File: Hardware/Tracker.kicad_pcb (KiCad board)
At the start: 2 copper layers, 233.7 x 114.2 mm, 58 parts, among them J1 Battery, J10 132134, J11 SPI_Programming, J2 Motor, J3 Wind, J4 RX, J5 TX, J6 GND, J7 GND, J8 GND, J9 Haeder_LED, U1 L7805, U2 ATmega328P-P, U3 LM317_TO-220, U4 L298N, U5 74HC123, U6 LM358, U7 GK9501, Y1 16MHz

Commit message: Update of PCB
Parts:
- removed D6: LED_RBKG, Connector_PinHeader_1.27mm:PinHeader_1x04_P1.27mm_Vertical
- removed R23: 270, Resistor_THT:R_Axial_DIN0204_L3.6mm_D1.6mm_P5.08mm_Horizontal
- added C10: 100nF, Capacitor_THT:C_Rect_L7.0mm_W2.0mm_P5.00mm, F.Cu at (82.3, 68.1)
- added D11: 1N5406, Diode_THT:D_DO-201AD_P15.24mm_Horizontal, F.Cu at (108.5, 116.6)
- added D12: 3.3V, Diode_THT:D_A-405_P10.16mm_Horizontal, F.Cu at (29.7, 86.9)
- added D13: LED, LED_THT:LED_D3.0mm, F.Cu at (54.9, 76.7)
- added J12: Sortie Moteur, TerminalBlock_Phoenix:TerminalBlock_Phoenix_MKDS-1,5-2-5.08_1x02_P5.08mm_Horizontal, F.Cu at (44.7, 127.3)
- added J13: Position_Potentiometer, TerminalBlock_Phoenix:TerminalBlock_Phoenix_MKDS-1,5-3-5.08_1x03_P5.08mm_Horizontal, F.Cu at (24.4, 76.2)
- added Q1: IRF4905, Package_TO_SOT_THT:TO-220-3_Vertical, F.Cu at (36.3, 102.4)
- added Q2: IRF520, Package_TO_SOT_THT:TO-220-3_Vertical, F.Cu at (34.2, 114.0)
- added Q4: IRF4905, Package_TO_SOT_THT:TO-220-3_Vertical, F.Cu at (61.5, 105.2)
- added Q5: IRF520, Package_TO_SOT_THT:TO-220-3_Vertical, F.Cu at (59.8, 113.9)
- added Q6: IRF4905, Package_TO_SOT_THT:TO-220-3_Vertical, F.Cu at (47.9, 90.9)
- added R13: 470, Resistor_THT:R_Axial_DIN0207_L6.3mm_D2.5mm_P7.62mm_Horizontal, F.Cu at (14.2, 103.4)
- added R16: 470, Resistor_THT:R_Axial_DIN0207_L6.3mm_D2.5mm_P7.62mm_Horizontal, F.Cu at (163.2, 103.8)
- added R17: 2.2K, Resistor_THT:R_Axial_DIN0207_L6.3mm_D2.5mm_P7.62mm_Horizontal, F.Cu at (27.9, 96.0)
- added R18: 1K, Resistor_THT:R_Axial_DIN0207_L6.3mm_D2.5mm_P7.62mm_Horizontal, F.Cu at (24.1, 104.9)
- added R19: 100k, Resistor_THT:R_Axial_DIN0207_L6.3mm_D2.5mm_P7.62mm_Horizontal, F.Cu at (30.5, 116.3)
- added R20: 1K, Resistor_THT:R_Axial_DIN0207_L6.3mm_D2.5mm_P7.62mm_Horizontal, F.Cu at (31.2, 96.0)
- added R24: 470, Resistor_THT:R_Axial_DIN0207_L6.3mm_D2.5mm_P7.62mm_Horizontal, F.Cu at (16.3, 124.0)
- added R26: 3.3K, Resistor_THT:R_Axial_DIN0207_L6.3mm_D2.5mm_P7.62mm_Horizontal, F.Cu at (37.3, 86.4)
- added R27: 470, Resistor_THT:R_Axial_DIN0207_L6.3mm_D2.5mm_P7.62mm_Horizontal, F.Cu at (75.2, 84.6)
- added R28: 1K, Resistor_THT:R_Axial_DIN0207_L6.3mm_D2.5mm_P7.62mm_Horizontal, F.Cu at (66.3, 97.8)
- added R29: 470, Resistor_THT:R_Axial_DIN0207_L6.3mm_D2.5mm_P7.62mm_Horizontal, F.Cu at (13.2, 124.0)
- added R30: 2.2K, Resistor_THT:R_Axial_DIN0207_L6.3mm_D2.5mm_P7.62mm_Horizontal, F.Cu at (66.0, 104.9)
- added R31: 1K, Resistor_THT:R_Axial_DIN0207_L6.3mm_D2.5mm_P7.62mm_Horizontal, F.Cu at (66.3, 115.6)
- added R32: 100k, Resistor_THT:R_Axial_DIN0207_L6.3mm_D2.5mm_P7.62mm_Horizontal, F.Cu at (66.5, 119.1)
- added R33: 1k, Resistor_THT:R_Axial_DIN0207_L6.3mm_D2.5mm_P7.62mm_Horizontal, F.Cu at (51.3, 91.9)
- added R34: 2.7K, Resistor_THT:R_Axial_DIN0207_L6.3mm_D2.5mm_P7.62mm_Horizontal, F.Cu at (26.7, 83.6)
- added R35: 1K, Resistor_THT:R_Axial_DIN0207_L6.3mm_D2.5mm_P7.62mm_Horizontal, F.Cu at (26.7, 86.6)
- added R37: 2.2K, Resistor_THT:R_Axial_DIN0207_L6.3mm_D2.5mm_P7.62mm_Horizontal, F.Cu at (54.4, 84.3)
- added R38: 3.3K, Resistor_THT:R_Axial_DIN0207_L6.3mm_D2.5mm_P7.62mm_Horizontal, F.Cu at (57.7, 76.7)
- added U10: PC817, Package_DIP:DIP-4_W7.62mm, F.Cu at (64.8, 91.2)
- added U11: PC817, Package_DIP:DIP-4_W7.62mm, F.Cu at (67.1, 122.9)
- added U12: PC817, Package_DIP:DIP-4_W7.62mm, F.Cu at (65.0, 84.3)
- added U8: PC817, Package_DIP:DIP-4_W7.62mm, F.Cu at (19.3, 116.8)
- D2, D3: value D -> 1N4818
- D4, D5, D8: value 1N4148 -> 1N5406; footprint Diode_THT:D_DO-35_SOD27_P7.62mm_Horizontal -> Diode_THT:D_DO-201AD_P15.24mm_Horizontal
- D9: value 1N4148 -> LED; footprint Diode_THT:D_DO-35_SOD27_P7.62mm_Horizontal -> LED_THT:LED_D3.0mm
- J2: value Motor -> +24V
- R1, R10, R11, R12, R15, R2, R3, R4, R5, R6, R7, R8, R9: footprint Resistor_THT:R_Axial_DIN0204_L3.6mm_D1.6mm_P5.08mm_Horizontal -> Resistor_THT:R_Axial_DIN0207_L6.3mm_D2.5mm_P7.62mm_Horizontal
- R21, R22: footprint Resistor_THT:R_Axial_DIN0204_L3.6mm_D1.6mm_P5.08mm_Horizontal -> Resistor_THT:R_Axial_DIN0207_L6.3mm_D2.5mm_P10.16mm_Horizontal
- U4: value L298N -> PC817; footprint Package_TO_SOT_THT:TO-220-15_P2.54x2.54mm_StaggerOdd_Lead4.58mm_Vertical -> Package_DIP:DIP-4_W7.62mm
- moved U4 199.4 mm to (17.3, 96.0), turned to 0 degrees
- moved D9 186.3 mm to (40.4, 85.3), turned to 0 degrees
- moved J2 174.7 mm to (47.8, 76.7)
- moved H4 134.4 mm to (9.91, 146.1)
- moved H1 132.9 mm to (10.9, 54.1)
- moved D5 111.8 mm to (108.2, 103.9), turned to 0 degrees
- moved D4 96.1 mm to (123.4, 122.7), turned to 180 degrees
- moved D8 93.7 mm to (123.4, 110.0), turned to 180 degrees
- moved C4 72.5 mm to (104.8, 67.5)
- moved C7 72.5 mm to (113.7, 83.3)
- moved J3 72.5 mm to (89.2, 73.5)
- moved R10 72.5 mm to (108.5, 78.6)
- moved R11 72.5 mm to (113.6, 80.9)
- moved R12 72.5 mm to (121.1, 80.8)
- moved R15 72.5 mm to (122.7, 67.6)
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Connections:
- net /XTAL1 renamed /Crystal/XTAl_1
- net /XTAL2 renamed /Crystal/XTAl_2
- D4 pad 1: +BATT -> Net-(D4-K)
- D4 pad 2: Net-(D4-A) -> GND
- D5 pad 1: Net-(D4-A) -> +VCC_Motor
- D5 pad 2: GND -> Net-(D4-K)
- D8 pad 1: +BATT -> Net-(D11-A)
- D8 pad 2: Net-(D8-A) -> GND
- D9 pad 1: Net-(D8-A) -> Net-(D9-K)
- D9 pad 2: GND -> +VCC_Motor
- J2 pad 1: Net-(D8-A) -> +24V
- J2 pad 2: Net-(D4-A) -> GND
- U2 pad 11: Net-(U2-PD5) -> unconnected-(U2-PD5-Pad11)
- U2 pad 12: Net-(U2-PD6) -> unconnected-(U2-PD6-Pad12)
- U2 pad 13: Net-(U2-PD7) -> unconnected-(U2-PD7-Pad13)
- U2 pad 14: /GNSS/RX -> /GNSS/PPS
- U2 pad 15: /GNSS/TX -> /GNSS/RX
- U2 pad 16: /GNSS/PPS -> /GNSS/TX
- U2 pad 23: /Motors/EN_MOTOR -> /Motors/IN_B
- U2 pad 24: /Motors/IN2_MOTOR -> /Motors/IN_A
- U2 pad 25: /Motors/IN1_MOTOR -> /Motors/ENABLE
- U2 pad 26: unconnected-(U2-PC3-Pad26) -> /Motors/Pot_Measure
- U4 pad 1: GND -> Net-(R13-Pad2)
- U4 pad 2: Net-(D8-A) -> GND
- U4 pad 3: Net-(D4-A) -> GND
- U4 pad 4: +5V -> Net-(R17-Pad1)
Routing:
- net +VCC_Motor: track 0.00 -> 62.7 mm
- net /Motors/EN_MOTOR: track 53.9 -> 0.00 mm
- net /Motors/IN_B: track 0.00 -> 53.3 mm
- net Net-(D11-A): track 0.00 -> 51.9 mm
- net Net-(D4-K): track 0.00 -> 49.6 mm
- net /Motors/IN_A: track 0.00 -> 46.0 mm
- net +24V: track 0.00 -> 45.4 mm
- net /Motors/IN1_MOTOR: track 32.7 -> 0.00 mm
- net /Motors/ENABLE: track 0.00 -> 32.7 mm
- net /Motors/IN2_MOTOR: track 32.7 -> 0.00 mm
- net (no net): track 0.00 -> 18.8 mm
- net Net-(Q2-G): track 0.00 -> 16.4 mm
- net GND: track 31.7 -> 16.7 mm
- net Net-(D4-A): track 12.3 -> 0.00 mm
- net Net-(D8-A): track 9.48 -> 0.00 mm
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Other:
- board size 233.7 x 114.2 mm -> 204.5 x 104.5 mm

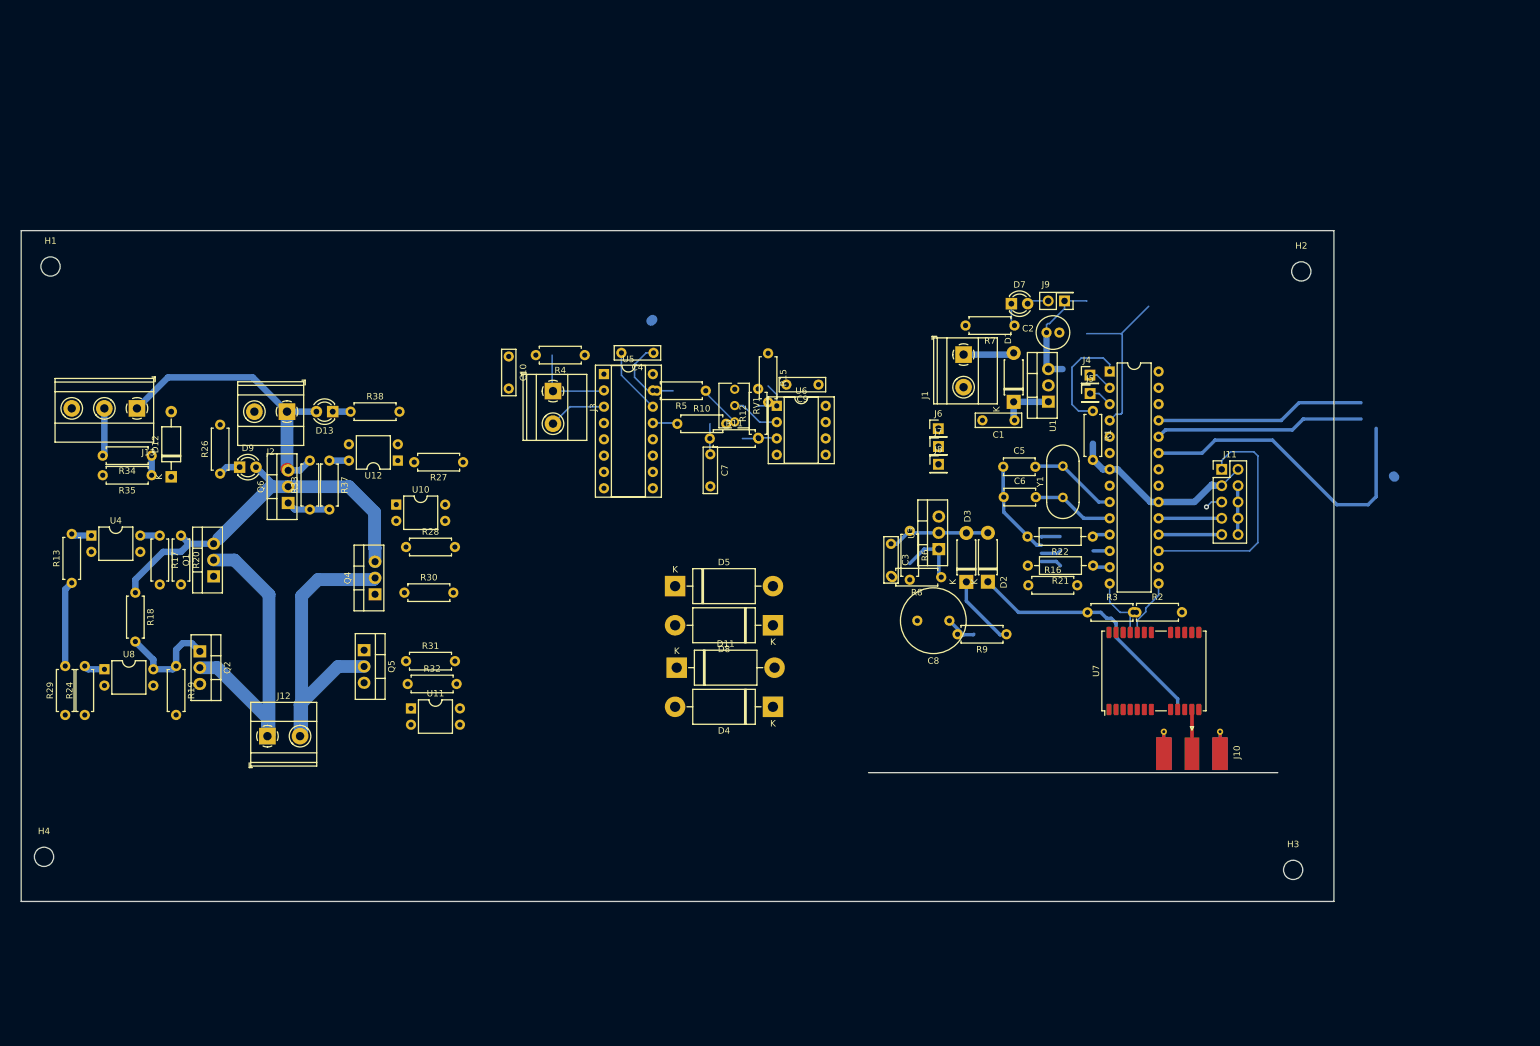
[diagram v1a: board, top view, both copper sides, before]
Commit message: Update PCB of Motor controller - version sent on production (debug purpose)
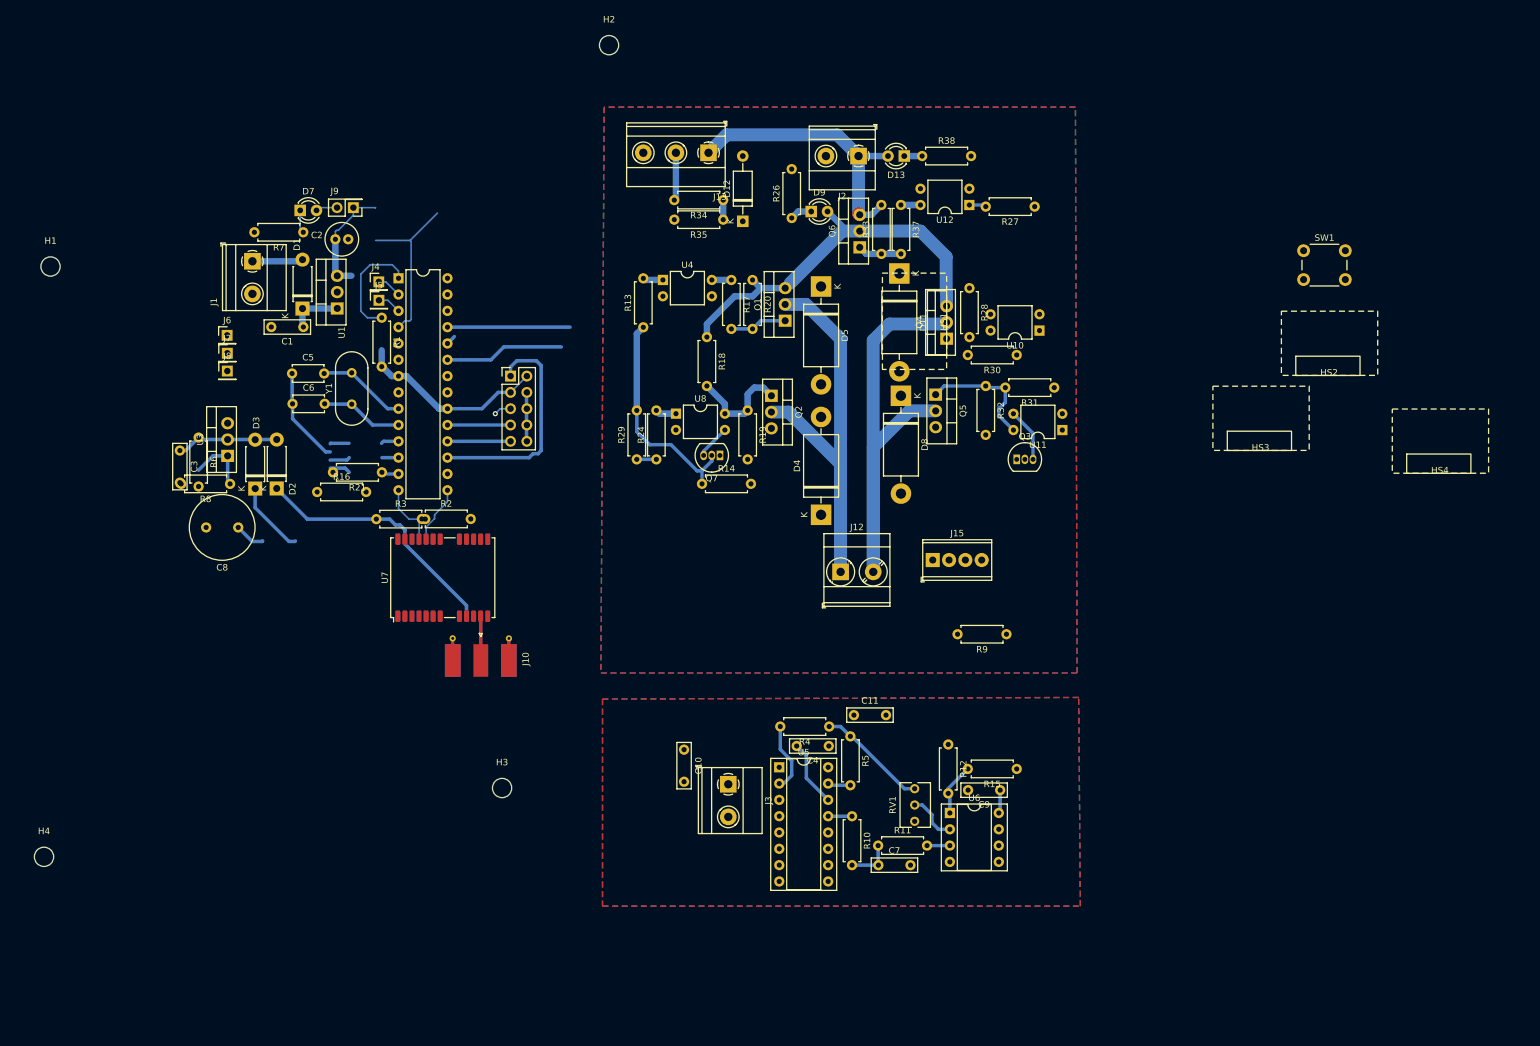
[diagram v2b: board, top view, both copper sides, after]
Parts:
- removed R22: 270, Resistor_THT:R_Axial_DIN0207_L6.3mm_D2.5mm_P10.16mm_Horizontal
- added C11: 100nF, Capacitor_THT:C_Rect_L7.0mm_W2.0mm_P5.00mm, F.Cu at (136.1, 124.0)
- added HS1: Heatsink, HeatSink:HeastSink_MOSFET_15mm_10mm_20mm, F.Cu at (150.6, 62.7)
- added HS2: Heatsink, HeatSink:HeastSink_MOSFET_15mm_10mm_20mm, F.Cu at (210.1, 71.1)
- added HS3: Heatsink, HeatSink:HeastSink_MOSFET_15mm_10mm_20mm, F.Cu at (199.4, 82.8)
- added HS4: Heatsink, HeatSink:HeastSink_MOSFET_15mm_10mm_20mm, F.Cu at (227.3, 86.4)
- added J15: Screw_Terminal_01x04, TerminalBlock_Phoenix:TerminalBlock_Phoenix_MPT-0,5-4-2.54_1x04_P2.54mm_Horizontal, F.Cu at (148.3, 99.8)
- added Q3: 2N7000, Package_TO_SOT_THT:TO-92_Inline, F.Cu at (161.4, 84.1)
- added Q7: 2N7000, Package_TO_SOT_THT:TO-92_Inline, F.Cu at (115.2, 83.5)
- added R14: 100k, Resistor_THT:R_Axial_DIN0207_L6.3mm_D2.5mm_P7.62mm_Horizontal, F.Cu at (112.4, 88.0)
- added SW1: SW_Push, Button_Switch_THT:SW_PUSH_6mm, F.Cu at (206.1, 51.6)
- J12: footprint TerminalBlock_Phoenix:TerminalBlock_Phoenix_MKDS-1,5-2-5.08_1x02_P5.08mm_Horizontal -> TerminalBlock_Phoenix:TerminalBlock_Phoenix_MKDS-3-2-5.08_1x02_P5.08mm_Horizontal
- R21: value 270 -> 100k; footprint Resistor_THT:R_Axial_DIN0207_L6.3mm_D2.5mm_P10.16mm_Horizontal -> Resistor_THT:R_Axial_DIN0207_L6.3mm_D2.5mm_P7.62mm_Horizontal
- moved H3 123.9 mm to (81.3, 135.3)
- moved H2 113.4 mm to (97.9, 19.6)
- moved C1 111.7 mm to (50.3, 63.5)
- moved D1 111.7 mm to (50.2, 60.7)
- moved J5 111.7 mm to (62.1, 59.4)
- moved R21 111.7 mm to (62.5, 86.2)
- moved R6 111.7 mm to (34.0, 80.7)
- moved U1 111.7 mm to (55.6, 60.6)
- moved C2 111.7 mm to (55.3, 49.9)
- moved C5 111.7 mm to (48.5, 70.8)
- moved C6 111.7 mm to (48.6, 75.5)
- moved D7 111.7 mm to (49.8, 45.4)
- moved J10 111.7 mm to (77.9, 113.7)
- moved J6 111.7 mm to (38.4, 64.8)
- moved R8 111.7 mm to (38.9, 88.0)
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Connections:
- C7 pad 2: GND -> GND_WIND
- C9 pad 2: GND -> GND_WIND
- D12 pad 2: GND -> GND_MOTOR
- D4 pad 2: GND -> GND_MOTOR
- D8 pad 2: GND -> GND_MOTOR
- J13 pad 3: GND -> GND_MOTOR
- J2 pad 2: GND -> GND_MOTOR
- J3 pad 2: GND -> GND_WIND
- Q2 pad 3: GND -> GND_MOTOR
- Q5 pad 1: Net-(Q5-G) -> Net-(Q3-D)
- Q5 pad 3: GND -> GND_MOTOR
- R15 pad 1: GND -> GND_WIND
- R18 pad 2: Net-(Q2-G) -> Net-(R18-Pad2)
- R19 pad 2: GND -> GND_MOTOR
- R21 pad 1: Net-(U2-PD7) -> /Motors/IN_B
- R21 pad 2: Net-(D6-RA) -> GND_MOTOR
- R24 pad 1: +5V -> /Motors/IN_B
- R24 pad 2: /Motors/IN_B -> Net-(R24-Pad2)
- R26 pad 2: GND -> GND_MOTOR
- R29 pad 1: +5V -> Net-(R29-Pad1)
- R31 pad 2: Net-(Q5-G) -> Net-(R31-Pad2)
- R32 pad 1: Net-(Q5-G) -> Net-(Q3-D)
- R32 pad 2: GND -> GND_MOTOR
- R35 pad 2: GND -> GND_MOTOR
- R38 pad 2: GND -> GND_MOTOR
- RV1 pad 3: GND -> GND_WIND
- U10 pad 2: GND -> GND_MOTOR
- U10 pad 3: GND -> GND_MOTOR
- U11 pad 1: /Motors/IN_A -> Net-(R29-Pad1)
- U11 pad 2: GND -> GND_MOTOR
- U11 pad 3: GND -> Net-(Q3-D)
- U11 pad 4: Net-(Q5-G) -> Net-(R31-Pad2)
- U12 pad 2: GND -> GND_MOTOR
- U12 pad 3: GND -> GND_MOTOR
- U4 pad 2: GND -> GND_MOTOR
- U4 pad 3: GND -> GND_MOTOR
- U5 pad 16: (no net) -> +5V
- U5 pad 3: GND -> GND_WIND
- U5 pad 8: (no net) -> GND_WIND
- U6 pad 4: GND -> GND_WIND
- U8 pad 1: /Motors/IN_B -> Net-(R24-Pad2)
- U8 pad 2: GND -> GND_MOTOR
- U8 pad 3: GND -> Net-(Q2-G)
- U8 pad 4: Net-(Q2-G) -> Net-(R18-Pad2)
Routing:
- net /Motors/IN_B: track 53.3 -> 21.6 mm
- net Net-(D4-K): track 49.6 -> 78.1 mm
- net Net-(D11-A): track 51.9 -> 80.1 mm
- net GND_MOTOR: track 0.00 -> 22.7 mm
- net +5V: track 54.5 -> 68.6 mm
- net /Motors/ENABLE: track 32.7 -> 19.1 mm
- net /Motors/IN_A: track 46.0 -> 35.9 mm
- net (no net): track 18.8 -> 8.77 mm
- net Net-(U5A-RCext): track 12.6 -> 3.57 mm
- net Net-(Q1-G): track 0.00 -> 8.91 mm
- net Net-(Q3-D): track 0.00 -> 8.37 mm
- net GND: track 16.7 -> 22.7 mm
- net Net-(Q2-G): track 16.4 -> 21.7 mm
- net Net-(R24-Pad2): track 0.00 -> 3.27 mm
- net Net-(D6-RA): track 3.24 -> 0.00 mm
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- added copper zone on B.Cu, net GND_MOTOR
- added copper zone on F.Cu, net GND_MOTOR
- added copper zone on B.Cu, net GND_WIND
- added copper zone on F.Cu, net GND_WIND
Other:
- board outline removed
